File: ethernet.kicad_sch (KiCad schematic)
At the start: 42 parts, among them U1 MPFS250T-FCVG484, U25 DP83867ISRGZR, Y3 Resonator_25MHz_ABM8G

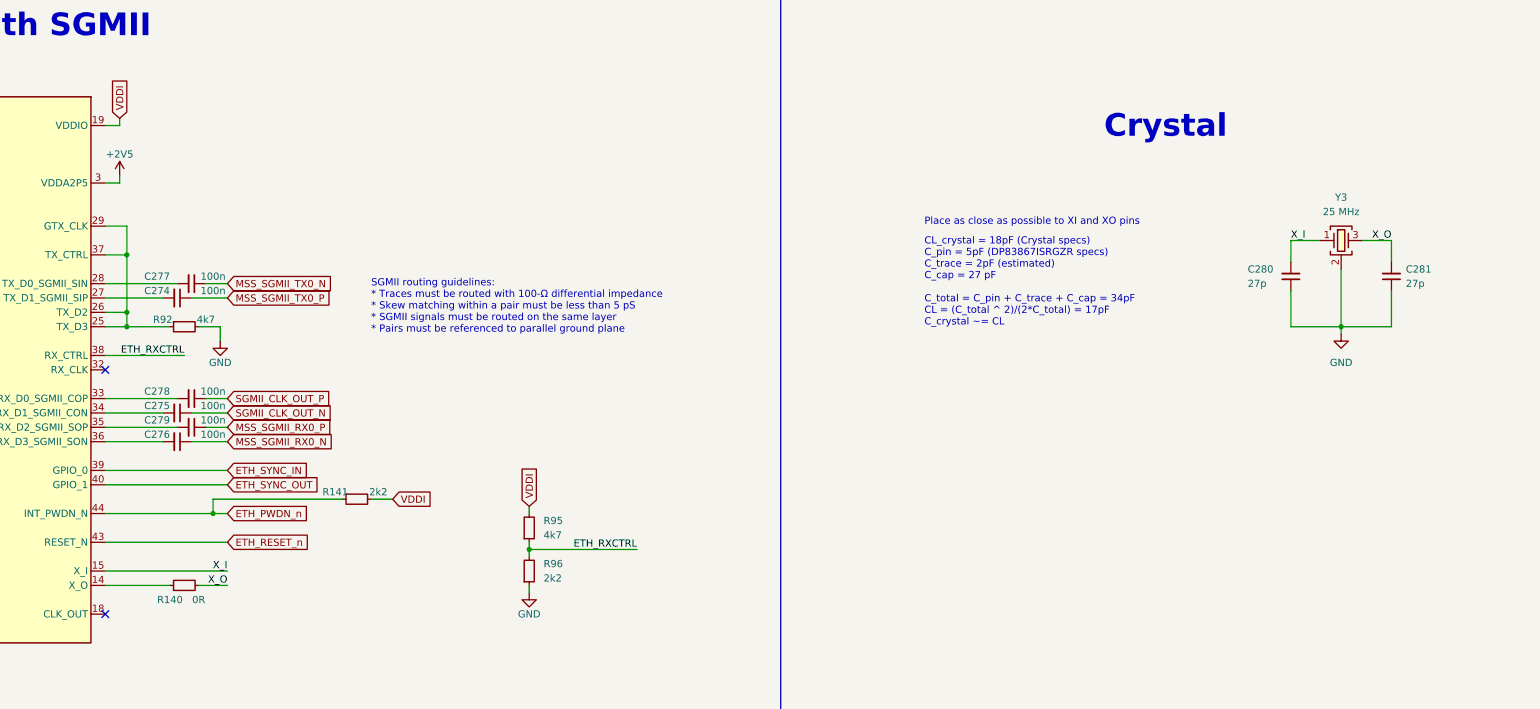
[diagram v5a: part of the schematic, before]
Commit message: [#55288] Change Ethernet PHY crystal to oscillator
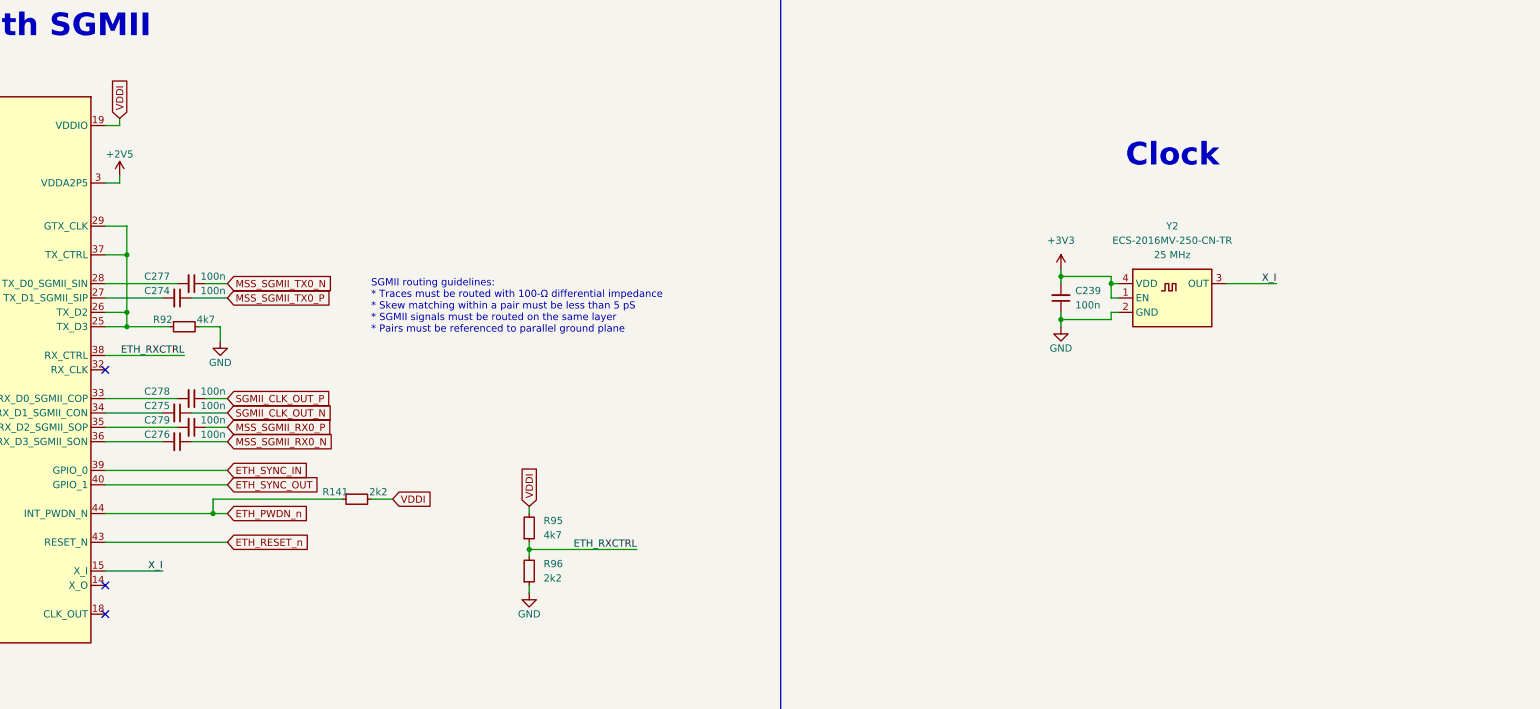
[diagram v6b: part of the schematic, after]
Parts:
- removed C280, C281: C_27p_0402, antmicro-footprints:C_0402_1005Metric, symbol antmicroCapacitors0402:C_27p_0402
- removed R140: R_0R_0201, antmicro-footprints:R_0201, symbol antmicroResistorsmisc:R_0R_0201
- removed Y3: Resonator_25MHz_ABM8G, antmicro-footprints:Oscillator_SMD_Geyer_KX-7-4Pin_3.2x2.5mm, symbol antmicroResonators:Resonator_25MHz_ABM8G
- added C239: C_100n_0201_25V, antmicro-footprints:C_0201, symbol antmicroCapacitorsmisc:C_100n_0201_25V
- added Y2: Oscillator_25MHz_ESC_2016MV, antmicro-footprints:Oscillator_SMD_ECS_2016MV_2x1.6x0.85mm, symbol antmicroOscillators:Oscillator_25MHz_ESC_2016MV
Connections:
- net GND: now also C239.1, Y2.2 (GND)
- net X_I: now also Y2.3 (OUT)
- new net +3V3: C239.2, Y2.1 (EN), Y2.4 (VDD)
- no-connect marks 7 -> 8
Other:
- note added: "Clock"
- note removed: "CL_crystal = 18pF (Crystal specs) C_pin = 5pF (DP83867ISRGZR specs) C_trace = 2pF (estimated) C_cap = 27 pF C_total = C_pin + C_trace + C_cap = 34pF CL = (C_total ^ 2)/(2*C_total) = 17pF C_crystal ~= CL"
- note removed: "Crystal"
- note removed: "Place as close as possible to XI and XO pins"
